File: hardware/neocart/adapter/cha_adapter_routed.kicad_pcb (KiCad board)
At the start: 2 copper layers, 173.9 x 134 mm, 53 parts, among them J2 FROM_PROG, U1 74HC165, U2 74HC165, U3 74HC165, U4 74HC165, U5 74HC165

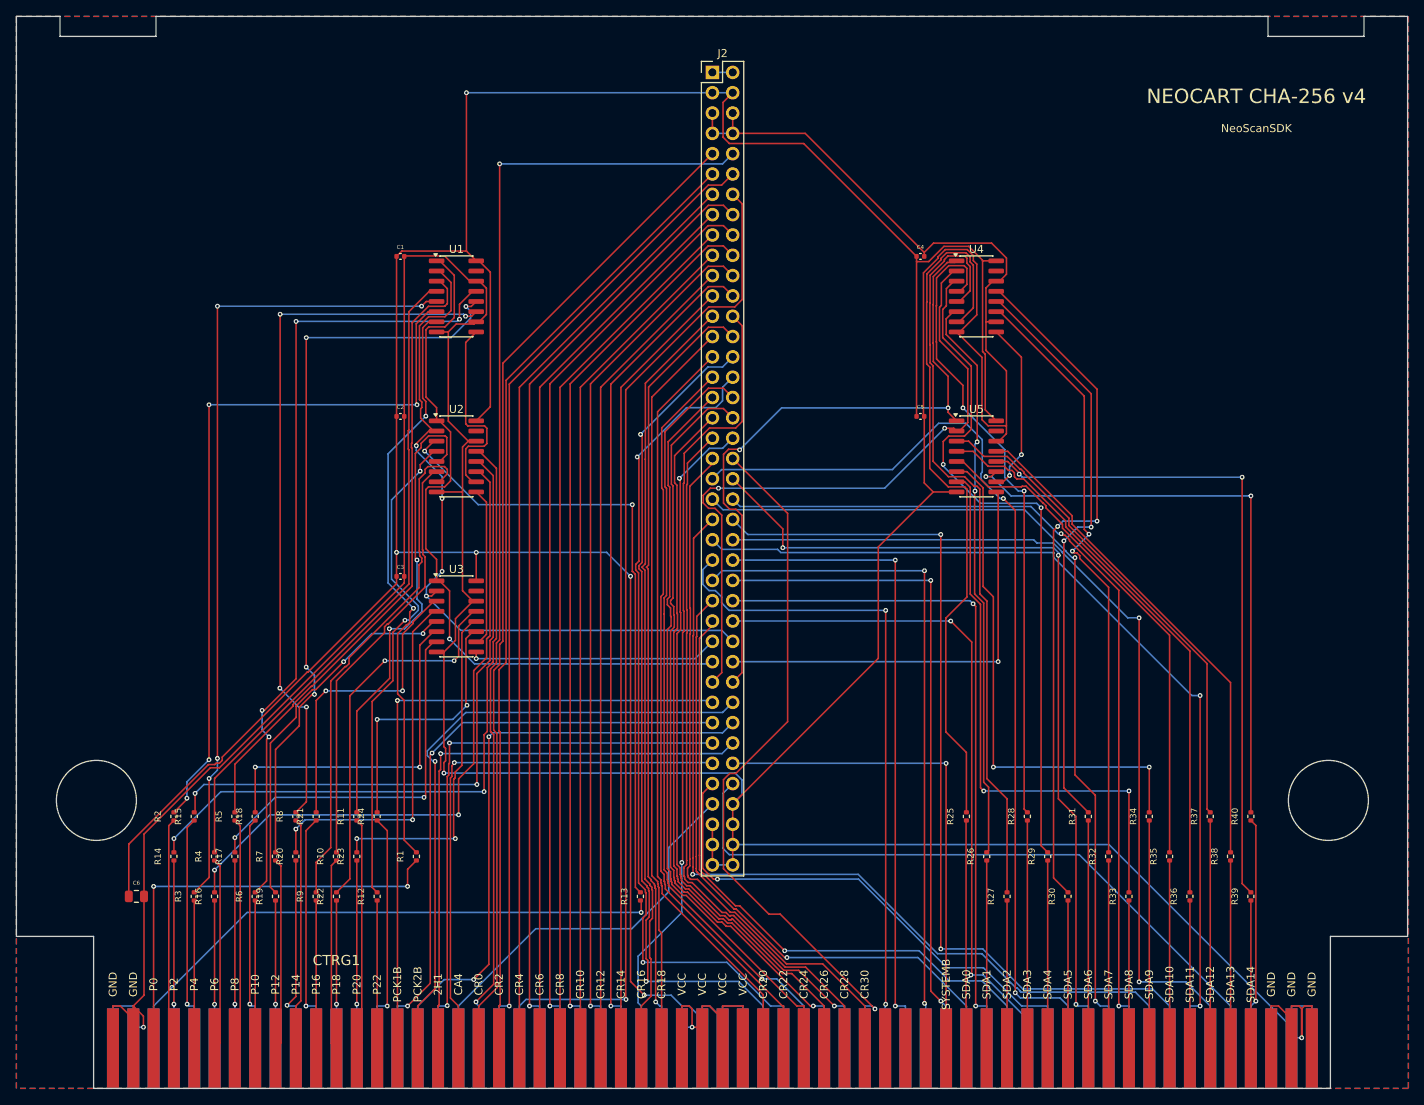
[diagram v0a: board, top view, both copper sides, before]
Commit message: NeoCart final routed PCBs + JLCPCB Gerbers — ready to order
Fixed J1 GND pins (60,62,64) from QMTech schematic — FPGA now has
ground through both headers. Re-routed with Freerouting 2.0.1 (Java 21,
multi-thread). GND routed as signal net, not just copper pour.

DRC clean:
- PROG: 143 violations (121 gold finger edge + 22 text cosmetic), 0 unconnected
- CHA:  152 violations (120 gold finger edge + 32 cosmetic), 0 unconnected
- 0 starved thermals, 0 shorts, 0 clearance errors

Chip verification: all 10 ICs power correct, all signal pins connected,
J1 GND confirmed on pins 60/62/64, J2 aligned between boards.

Gerbers: neocart_prog_gerbers.zip, neocart_cha_gerbers.zip
Order settings: 2-layer, 1.6mm, ENIG, gold fingers Yes, 45° chamfer.

Co-Authored-By: Claude Opus 4.6 (1M context) <noreply@anthropic.com>
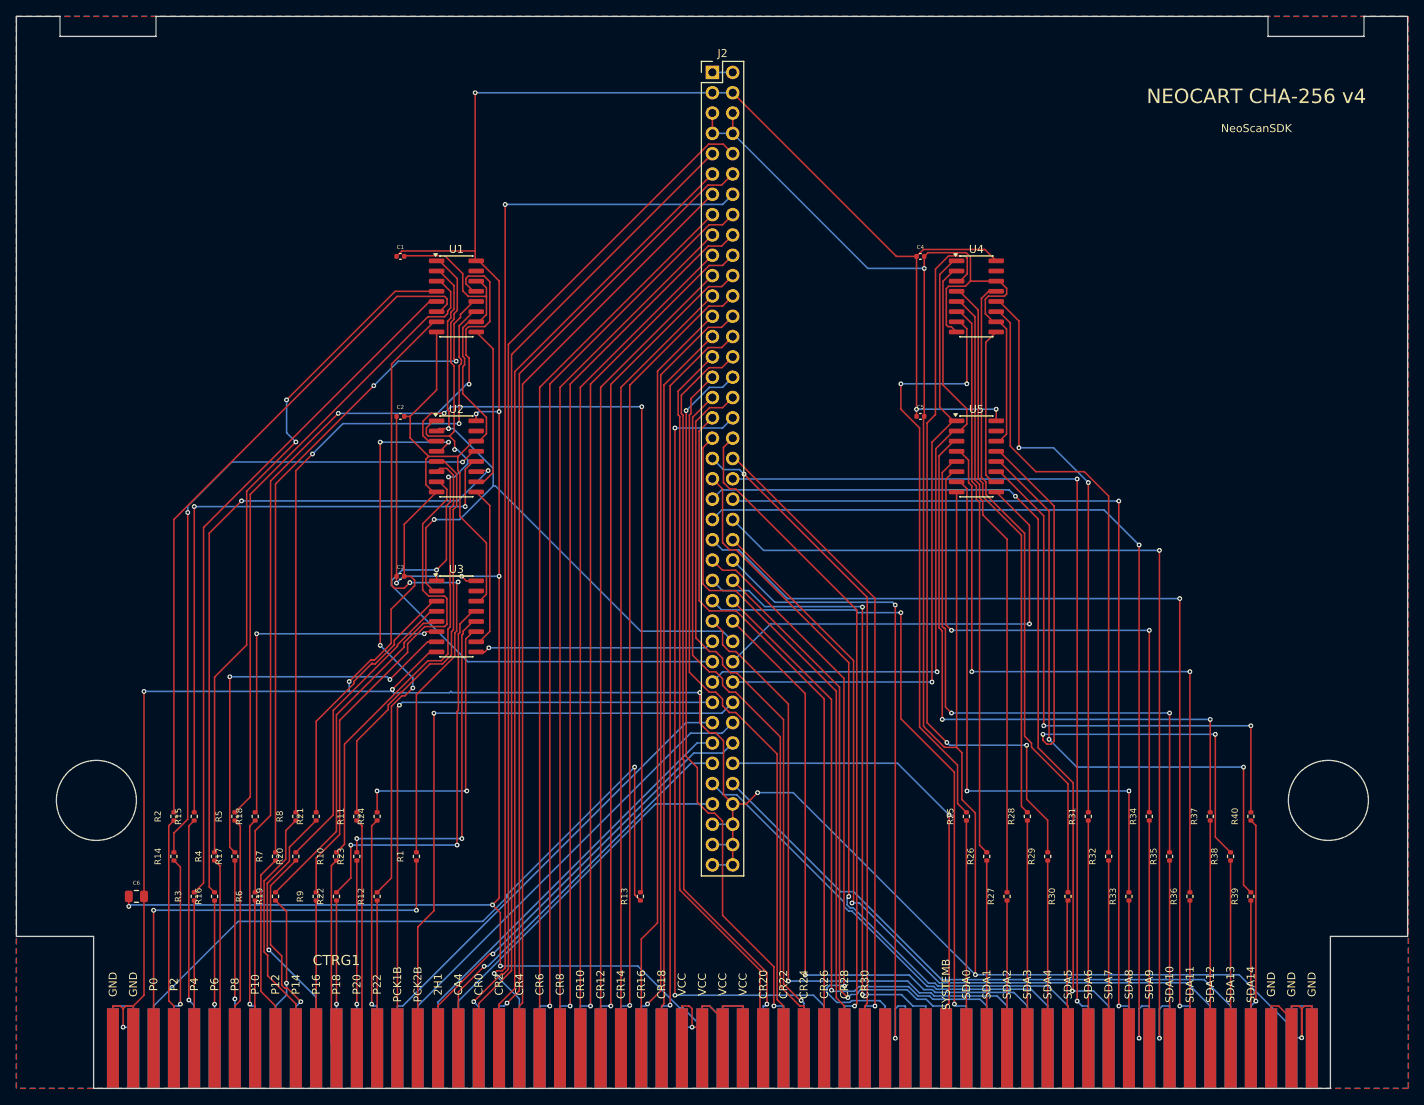
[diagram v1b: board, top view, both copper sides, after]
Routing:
- net GND: track 604.8 -> 643.3 mm, vias 3 -> 9
- net VCC_5V: track 427.7 -> 404.5 mm, vias 6 -> 12
- net P1: track 72.6 -> 95.0 mm
- net SDD0: track 121.2 -> 99.0 mm, vias 2 -> 1
- net SDA12_R: track 62.2 -> 81.2 mm, vias 0 -> 2
- net CLK8M: track 72.3 -> 53.5 mm, vias 2 -> 0
- net SIG_2H1: track 74.0 -> 55.8 mm
- net SDA2_R: track 94.8 -> 76.7 mm
- net CHA_CA4: track 68.6 -> 50.6 mm
- net CLK24M: track 76.1 -> 59.3 mm, vias 2 -> 0
- net CLK12M: track 76.0 -> 59.3 mm, vias 2 -> 0
- net SDA13_R: track 63.1 -> 79.0 mm, vias 0 -> 2
- net SDA0_R: track 88.9 -> 73.7 mm, vias 0 -> 2
- net P4_R: track 102.1 -> 86.9 mm, vias 4 -> 0
- net SDA10_R: track 63.3 -> 77.6 mm, vias 0 -> 2
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
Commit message: CHA v4 with PinSocket + PROG v5 BGA attempt
CHA v4: PinSocket footprint for J2, clean DRC (0 unconnected, 0 shorts),
LCSC fields embedded, JLCPCB plugin generates correct CPL with pad-center
coordinates. Ready for JLCPCB order.

PROG v5 BGA-256: routing failed — 122 unrouted nets after 15 passes on
two different placement attempts. Freerouting can't handle BGA fanout.
Need TQFP-144 fallback or professional BGA routing tool.

Lessons: PinSocket footprint mirrors pin 2 column. For parallel board
stacking, use PinHeader pads + socket LCSC part. JLCPCB CPL needs
pad-center coordinates (not footprint origin).

Co-Authored-By: Claude Opus 4.6 (1M context) <noreply@anthropic.com>
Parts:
- J2: footprint PinHeader_2x40_P2.54mm_Vertical -> PinSocket_2x40_P2.54mm_Vertical
- moved J2 3.00 mm to (90.0, 7.00)
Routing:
- net VCC_5V: track 404.5 -> 453.2 mm, vias 12 -> 5
- net GND: track 643.3 -> 607.3 mm, vias 9 -> 11
- net SDA5_R: track 80.9 -> 101.7 mm, vias 0 -> 4
- net CR5: track 136.7 -> 117.0 mm, vias 2 -> 1
- net CLK12M: track 59.3 -> 77.8 mm, vias 0 -> 2
- net P5_R: track 78.5 -> 61.6 mm
- net P7_R: track 84.8 -> 68.5 mm
- net SDD4: track 127.7 -> 111.5 mm
- net P12_R: track 83.9 -> 99.9 mm, vias 2 -> 4
- net SDA4_R: track 93.7 -> 79.6 mm
- net SDD5: track 126.3 -> 112.9 mm, vias 2 -> 1
- net SDD7: track 107.2 -> 120.5 mm
- net SSR1_OUT: track 20.1 -> 32.5 mm, vias 0 -> 2
- net P11_R: track 45.0 -> 32.8 mm, vias 2 -> 0
- net FIX7: track 82.7 -> 94.5 mm
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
